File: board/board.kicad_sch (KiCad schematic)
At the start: 3 parts, among them J1 022_battery_cells, J2 011_GPIO

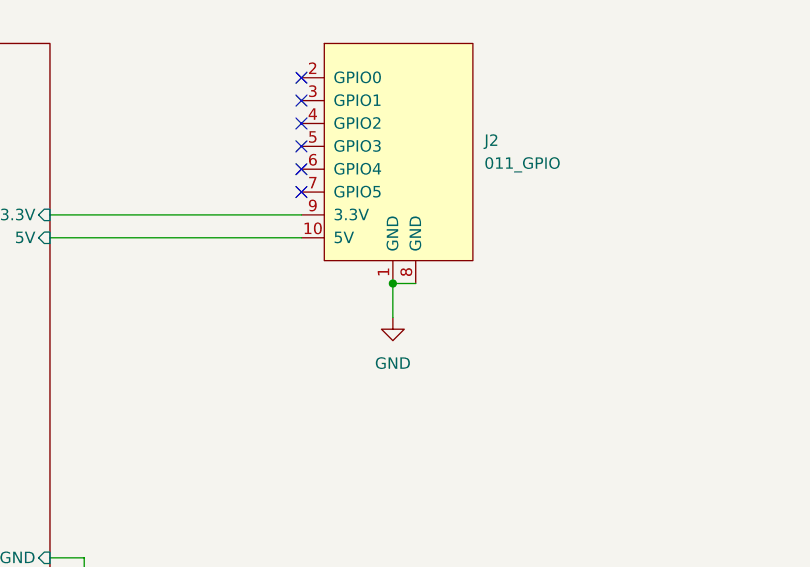
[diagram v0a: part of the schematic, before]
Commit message: switched edge connectors to use the correct footprints and renamed local libraries to fit with the edgy naming convention
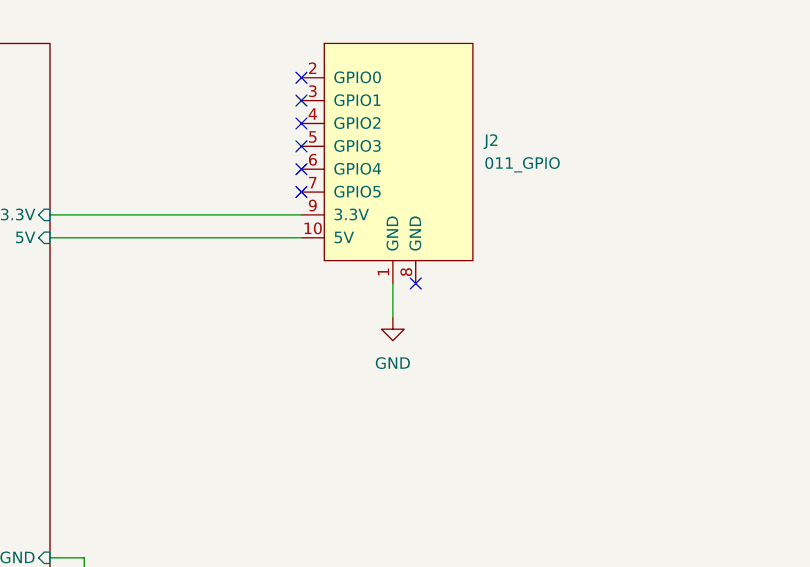
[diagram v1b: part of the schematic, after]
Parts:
- J1: footprint on_edge:debug_edge_2x05_device -> on_edge:on_edge_2x05_device
- J2: footprint on_edge:debug_edge_2x05_host -> on_edge:on_edge_2x05_host
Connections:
- net GND: no longer J2.8 (GND)
- no-connect marks 9 -> 10
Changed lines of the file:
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@@
 (kicad_sch (version 20211123) (generator eeschema)
   (paper "A4")
-  (junction (at 213.36 99.06) (diameter 0) (color 0 0 0 0)
-  )
   (no_connect (at 203.2 86.36))
   (no_connect (at 203.2 76.2))
@@
   (no_connect (at 87.63 86.36))
   (no_connect (at 87.63 83.82))
+  (no_connect (at 215.9 99.06))
   (no_connect (at 87.63 78.74))
   (no_connect (at 203.2 78.74))
@@
     (stroke (width 0) (type default) (color 0 0 0 0))
   )
-  (wire (pts (xy 213.36 99.06) (xy 215.9 99.06))
-    (stroke (width 0) (type default) (color 0 0 0 0))
-  )
   (wire (pts (xy 213.36 99.06) (xy 213.36 102.87))
     (stroke (width 0) (type default) (color 0 0 0 0))
@@
     (property "Reference" "J1" (id 0) (at 76.835 67.31 0))
     (property "Value" "022_battery_cells" (id 1) (at 76.835 69.85 0))
-    (property "Footprint" "on_edge:debug_edge_2x05_device" (id 2) (at 68.58 68.58 0)
+    (property "Footprint" "on_edge:on_edge_2x05_device" (id 2) (at 68.58 68.58 0)
       (effects (font (size 1.27 1.27)) hide)
     )
@@
       (effects (font (size 1.27 1.27)) (justify left))
     )
-    (property "Footprint" "on_edge:debug_edge_2x05_host" (id 2) (at 222.25 68.58 0)
+    (property "Footprint" "on_edge:on_edge_2x05_host" (id 2) (at 222.25 68.58 0)
       (effects (font (size 1.27 1.27)) hide)
     )
@@
     )
     (path "/767ce4c6-0e55-4543-92f0-34cb8237a544/875404be-e359-458a-af29-1bd3403dd55f"
-      (reference "C2") (unit 1) (value "TPSE107K016R0100") (footprint "stpup:CAPMP7344X43-T_V")
+      (reference "C2") (unit 1) (value "TPSE107K016R0100") (footprint "b132:CAPMP7344X43-T_V")
     )
     (path "/767ce4c6-0e55-4543-92f0-34cb8237a544/301727b6-248b-4eb4-8c37-cb369ee1a241"
-      (reference "C3") (unit 1) (value "TPSE107K016R0100") (footprint "stpup:CAPMP7344X43-T_V")
+      (reference "C3") (unit 1) (value "TPSE107K016R0100") (footprint "b132:CAPMP7344X43-T_V")
     )
     (path "/767ce4c6-0e55-4543-92f0-34cb8237a544/78ce8c1e-89e0-4419-807a-81faccaa13a1"
@@
     )
     (path "/767ce4c6-0e55-4543-92f0-34cb8237a544/d618158f-4184-4754-aa33-65a98e706342"
-      (reference "D1") (unit 1) (value "PMEG100V100ELPDAZ") (footprint "stpup:PMEG100V100ELPDAZ")
+      (reference "D1") (unit 1) (value "PMEG100V100ELPDAZ") (footprint "b132:PMEG100V100ELPDAZ")
     )
     (path "/767ce4c6-0e55-4543-92f0-34cb8237a544/7b1add24-b218-4ce0-80c1-f1e7a71c0711"
@@
     )
     (path "/3787921c-1252-47a4-a46e-7281e360658c"
-      (reference "J1") (unit 1) (value "022_battery_cells") (footprint "on_edge:debug_edge_2x05_device")
+      (reference "J1") (unit 1) (value "022_battery_cells") (footprint "on_edge:on_edge_2x05_device")
     )
     (path "/f9be9108-23a2-4fb6-b407-8be8eef9497e"
-      (reference "J2") (unit 1) (value "011_GPIO") (footprint "on_edge:debug_edge_2x05_host")
+      (reference "J2") (unit 1) (value "011_GPIO") (footprint "on_edge:on_edge_2x05_host")
     )
     (path "/767ce4c6-0e55-4543-92f0-34cb8237a544/58b75830-9e39-45c9-8547-367ebee8a907"
-      (reference "L1") (unit 1) (value "4.7uH") (footprint "stpup:WURTH 5040")
+      (reference "L1") (unit 1) (value "4.7uH") (footprint "b132:WURTH 5040")
     )
     (path "/b72b6f4a-7489-40f2-bb90-d75ae01aa368"
@@
     )
     (path "/767ce4c6-0e55-4543-92f0-34cb8237a544/7de04273-7eda-4419-ad6c-938bfee9f2d2"
-      (reference "U1") (unit 1) (value "LM2623LDX/NOPB") (footprint "stpup:NHE0014A_V")
-    )
-  )
+      (reference "U1") (unit 1) (value "LM2623LDX/NOPB") (footprint "b132:NHE0014A_V")
+    )
+  )

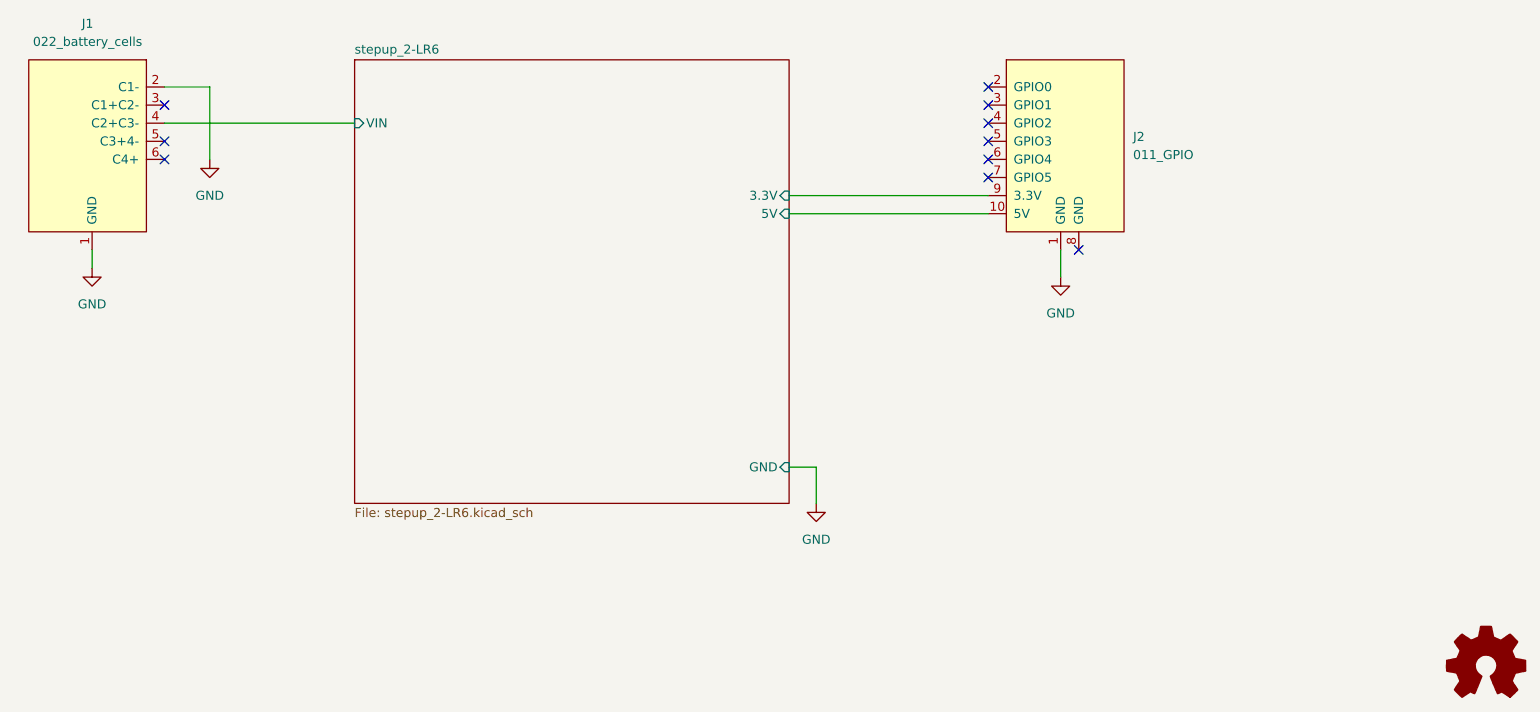
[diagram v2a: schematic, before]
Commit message: switched to ceramic caps
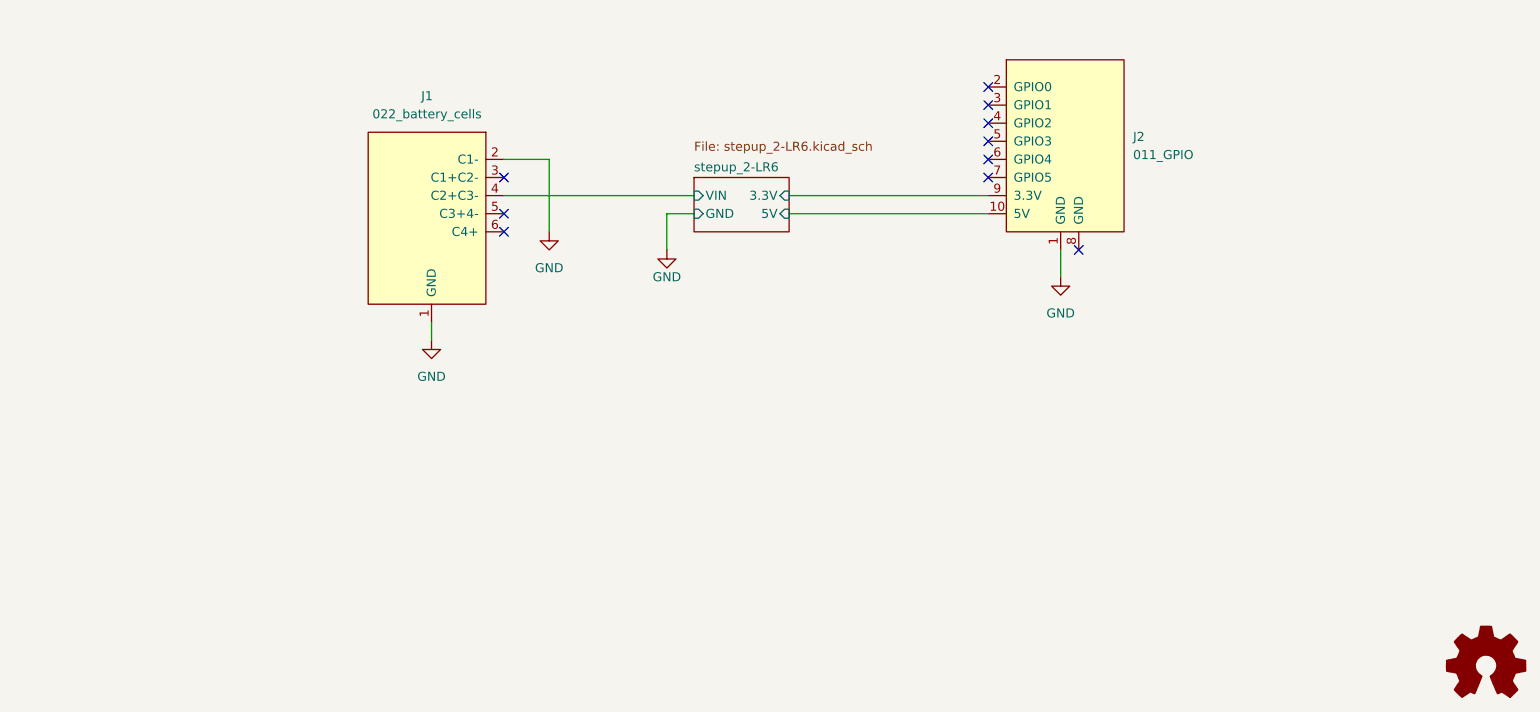
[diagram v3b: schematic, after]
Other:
- moved on the sheet: J1
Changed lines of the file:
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@@
   (no_connect (at 203.2 76.2))
   (no_connect (at 203.2 83.82))
-  (no_connect (at 87.63 86.36))
-  (no_connect (at 87.63 83.82))
+  (no_connect (at 135.255 96.52))
+  (no_connect (at 135.255 93.98))
   (no_connect (at 215.9 99.06))
-  (no_connect (at 87.63 78.74))
+  (no_connect (at 135.255 88.9))
   (no_connect (at 203.2 78.74))
   (no_connect (at 203.2 88.9))
   (no_connect (at 203.2 81.28))
-  (wire (pts (xy 93.98 76.2) (xy 93.98 86.36))
+  (wire (pts (xy 141.605 86.36) (xy 141.605 96.52))
     (stroke (width 0) (type default) (color 0 0 0 0))
   )
@@
     (stroke (width 0) (type default) (color 0 0 0 0))
   )
-  (wire (pts (xy 179.07 129.54) (xy 175.26 129.54))
-    (stroke (width 0) (type default) (color 0 0 0 0))
-  )
-  (wire (pts (xy 77.47 99.06) (xy 77.47 101.6))
-    (stroke (width 0) (type default) (color 0 0 0 0))
-  )
-  (wire (pts (xy 87.63 81.28) (xy 114.3 81.28))
+  (wire (pts (xy 158.115 93.98) (xy 161.925 93.98))
+    (stroke (width 0) (type default) (color 0 0 0 0))
+  )
+  (wire (pts (xy 125.095 109.22) (xy 125.095 111.76))
+    (stroke (width 0) (type default) (color 0 0 0 0))
+  )
+  (wire (pts (xy 135.255 91.44) (xy 161.925 91.44))
     (stroke (width 0) (type default) (color 0 0 0 0))
   )
@@
     (stroke (width 0) (type default) (color 0 0 0 0))
   )
-  (wire (pts (xy 87.63 76.2) (xy 93.98 76.2))
+  (wire (pts (xy 135.255 86.36) (xy 141.605 86.36))
     (stroke (width 0) (type default) (color 0 0 0 0))
   )
@@
     (stroke (width 0) (type default) (color 0 0 0 0))
   )
-  (wire (pts (xy 179.07 134.62) (xy 179.07 129.54))
-    (stroke (width 0) (type default) (color 0 0 0 0))
-  )
-  (symbol (lib_id "power:GND") (at 77.47 101.6 0) (unit 1)
-    (in_bom yes) (on_board yes) (fields_autoplaced)
-    (property "Reference" "#PWR0102" (id 0) (at 77.47 107.95 0)
-      (effects (font (size 1.27 1.27)) hide)
-    )
-    (property "Value" "GND" (id 1) (at 77.47 106.68 0))
-    (property "Footprint" "" (id 2) (at 77.47 101.6 0)
-      (effects (font (size 1.27 1.27)) hide)
-    )
-    (property "Datasheet" "" (id 3) (at 77.47 101.6 0)
-      (effects (font (size 1.27 1.27)) hide)
-    )
-    (pin "1")
-  )
-  (symbol (lib_id "put_on_edge:022_battery_cells") (at 76.2 85.09 0) (mirror y) (unit 1)
-    (in_bom yes) (on_board yes) (fields_autoplaced)
-    (property "Reference" "J1" (id 0) (at 76.835 67.31 0))
-    (property "Value" "022_battery_cells" (id 1) (at 76.835 69.85 0))
-    (property "Footprint" "on_edge:on_edge_2x05_device" (id 2) (at 68.58 68.58 0)
-      (effects (font (size 1.27 1.27)) hide)
-    )
-    (property "Datasheet" "" (id 3) (at 68.58 68.58 0)
+  (wire (pts (xy 158.115 99.06) (xy 158.115 93.98))
+    (stroke (width 0) (type default) (color 0 0 0 0))
+  )
+  (symbol (lib_id "power:GND") (at 125.095 111.76 0) (unit 1)
+    (in_bom yes) (on_board yes) (fields_autoplaced)
+    (property "Reference" "#PWR0102" (id 0) (at 125.095 118.11 0)
+      (effects (font (size 1.27 1.27)) hide)
+    )
+    (property "Value" "GND" (id 1) (at 125.095 116.84 0))
+    (property "Footprint" "" (id 2) (at 125.095 111.76 0)
+      (effects (font (size 1.27 1.27)) hide)
+    )
+    (property "Datasheet" "" (id 3) (at 125.095 111.76 0)
+      (effects (font (size 1.27 1.27)) hide)
+    )
+    (pin "1")
+  )
+  (symbol (lib_id "put_on_edge:022_battery_cells") (at 123.825 95.25 0) (mirror y) (unit 1)
+    (in_bom yes) (on_board yes) (fields_autoplaced)
+    (property "Reference" "J1" (id 0) (at 124.46 77.47 0))
+    (property "Value" "022_battery_cells" (id 1) (at 124.46 80.01 0))
+    (property "Footprint" "on_edge:on_edge_2x05_device" (id 2) (at 116.205 78.74 0)
+      (effects (font (size 1.27 1.27)) hide)
+    )
+    (property "Datasheet" "" (id 3) (at 116.205 78.74 0)
       (effects (font (size 1.27 1.27)) hide)
     )
@@
     (pin "1")
   )
-  (symbol (lib_id "power:GND") (at 179.07 134.62 0) (unit 1)
-    (in_bom yes) (on_board yes) (fields_autoplaced)
-    (property "Reference" "#PWR0101" (id 0) (at 179.07 140.97 0)
-      (effects (font (size 1.27 1.27)) hide)
-    )
-    (property "Value" "GND" (id 1) (at 179.07 139.7 0))
-    (property "Footprint" "" (id 2) (at 179.07 134.62 0)
-      (effects (font (size 1.27 1.27)) hide)
-    )
-    (property "Datasheet" "" (id 3) (at 179.07 134.62 0)
+  (symbol (lib_id "power:GND") (at 158.115 99.06 0) (mirror y) (unit 1)
+    (in_bom yes) (on_board yes)
+    (property "Reference" "#PWR0101" (id 0) (at 158.115 105.41 0)
+      (effects (font (size 1.27 1.27)) hide)
+    )
+    (property "Value" "GND" (id 1) (at 158.115 102.87 0))
+    (property "Footprint" "" (id 2) (at 158.115 99.06 0)
+      (effects (font (size 1.27 1.27)) hide)
+    )
+    (property "Datasheet" "" (id 3) (at 158.115 99.06 0)
       (effects (font (size 1.27 1.27)) hide)
     )
@@
     )
   )
-  (symbol (lib_id "power:GND") (at 93.98 86.36 0) (unit 1)
-    (in_bom yes) (on_board yes) (fields_autoplaced)
-    (property "Reference" "#PWR0103" (id 0) (at 93.98 92.71 0)
-      (effects (font (size 1.27 1.27)) hide)
-    )
-    (property "Value" "GND" (id 1) (at 93.98 91.44 0))
-    (property "Footprint" "" (id 2) (at 93.98 86.36 0)
-      (effects (font (size 1.27 1.27)) hide)
-    )
-    (property "Datasheet" "" (id 3) (at 93.98 86.36 0)
+  (symbol (lib_id "power:GND") (at 141.605 96.52 0) (unit 1)
+    (in_bom yes) (on_board yes) (fields_autoplaced)
+    (property "Reference" "#PWR0103" (id 0) (at 141.605 102.87 0)
+      (effects (font (size 1.27 1.27)) hide)
+    )
+    (property "Value" "GND" (id 1) (at 141.605 101.6 0))
+    (property "Footprint" "" (id 2) (at 141.605 96.52 0)
+      (effects (font (size 1.27 1.27)) hide)
+    )
+    (property "Datasheet" "" (id 3) (at 141.605 96.52 0)
       (effects (font (size 1.27 1.27)) hide)
     )
@@
     (pin "9")
   )
-  (sheet (at 114.3 72.39) (size 60.96 62.23) (fields_autoplaced)
+  (sheet (at 161.925 88.9) (size 13.335 7.62)
     (stroke (width 0.1524) (type solid) (color 0 0 0 0))
     (fill (color 0 0 0 0.0000))
-    (property "Sheet name" "stepup_2-LR6" (id 0) (at 114.3 71.6784 0)
+    (property "Sheet name" "stepup_2-LR6" (id 0) (at 161.925 88.1884 0)
       (effects (font (size 1.27 1.27)) (justify left bottom))
     )
-    (property "Sheet file" "stepup_2-LR6.kicad_sch" (id 1) (at 114.3 135.2046 0)
+    (property "Sheet file" "stepup_2-LR6.kicad_sch" (id 1) (at 161.925 83.82 0)
       (effects (font (size 1.27 1.27)) (justify left top))
     )
-    (pin "GND" input (at 175.26 129.54 0)
-      (effects (font (size 1.27 1.27)) (justify right))
-    )
-    (pin "VIN" input (at 114.3 81.28 180)
+    (pin "GND" input (at 161.925 93.98 180)
+      (effects (font (size 1.27 1.27)) (justify left))
+    )
+    (pin "VIN" input (at 161.925 91.44 180)
       (effects (font (size 1.27 1.27)) (justify left))
     )
@@
       (reference "C1") (unit 1) (value "4.7pF") (footprint "Capacitor_SMD:C_0402_1005Metric")
     )
-    (path "/767ce4c6-0e55-4543-92f0-34cb8237a544/875404be-e359-458a-af29-1bd3403dd55f"
-      (reference "C2") (unit 1) (value "TPSE107K016R0100") (footprint "b132:CAPMP7344X43-T_V")
-    )
-    (path "/767ce4c6-0e55-4543-92f0-34cb8237a544/301727b6-248b-4eb4-8c37-cb369ee1a241"
-      (reference "C3") (unit 1) (value "TPSE107K016R0100") (footprint "b132:CAPMP7344X43-T_V")
+    (path "/767ce4c6-0e55-4543-92f0-34cb8237a544/ea63d2fa-73f5-48cb-a45b-3d9595b2371a"
+      (reference "C2") (unit 1) (value "22uF") (footprint "Capacitor_SMD:C_0805_2012Metric")
+    )
+    (path "/767ce4c6-0e55-4543-92f0-34cb8237a544/08899149-8f1d-49fe-966f-12ab5c9966a5"
+      (reference "C3") (unit 1) (value "22uF") (footprint "Capacitor_SMD:C_0805_2012Metric")
     )
     (path "/767ce4c6-0e55-4543-92f0-34cb8237a544/78ce8c1e-89e0-4419-807a-81faccaa13a1"
@@
       (reference "C7") (unit 1) (value "33pF") (footprint "Capacitor_SMD:C_0603_1608Metric")
     )
+    (path "/767ce4c6-0e55-4543-92f0-34cb8237a544/3d4b9684-a268-4a9d-9665-12d40b24f50b"
+      (reference "C8") (unit 1) (value "22uF") (footprint "Capacitor_SMD:C_0805_2012Metric")
+    )
+    (path "/767ce4c6-0e55-4543-92f0-34cb8237a544/686a2fc2-958f-4786-b4e3-5d42afd80c77"
+      (reference "C9") (unit 1) (value "22uF") (footprint "Capacitor_SMD:C_0805_2012Metric")
+    )
     (path "/767ce4c6-0e55-4543-92f0-34cb8237a544/d618158f-4184-4754-aa33-65a98e706342"
